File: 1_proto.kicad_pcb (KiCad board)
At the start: 2 copper layers, 229.5 x 77.5 mm, 106 parts, among them K1 KEYSW, K10 KEYSW, K11 KEYSW, K12 KEYSW, K13 KEYSW, K14 KEYSW, K15 KEYSW, K16 KEYSW, K17 KEYSW, K18 KEYSW, K19 KEYSW, K2 KEYSW, K20 KEYSW, K21 KEYSW, K22 KEYSW, K23 KEYSW, K24 KEYSW, K24-A1 KEYSW, K25 KEYSW, K26 KEYSW, K27 KEYSW, K28 KEYSW, K29 KEYSW, K3 KEYSW, K30 KEYSW, K31 KEYSW, K32 KEYSW, K33 KEYSW, K34 KEYSW, K35 KEYSW, K36 KEYSW, K37 KEYSW, K38 KEYSW, K39 KEYSW, K4 KEYSW, K40 KEYSW, K41 KEYSW, K42 KEYSW, K43 KEYSW, K44 KEYSW, K45 KEYSW, K46 KEYSW, K47 KEYSW, K48 KEYSW, K5 KEYSW, K6 KEYSW, K7 KEYSW, K8 KEYSW, K9 KEYSW, SW1 SW_PUSH, U1 ProMicro

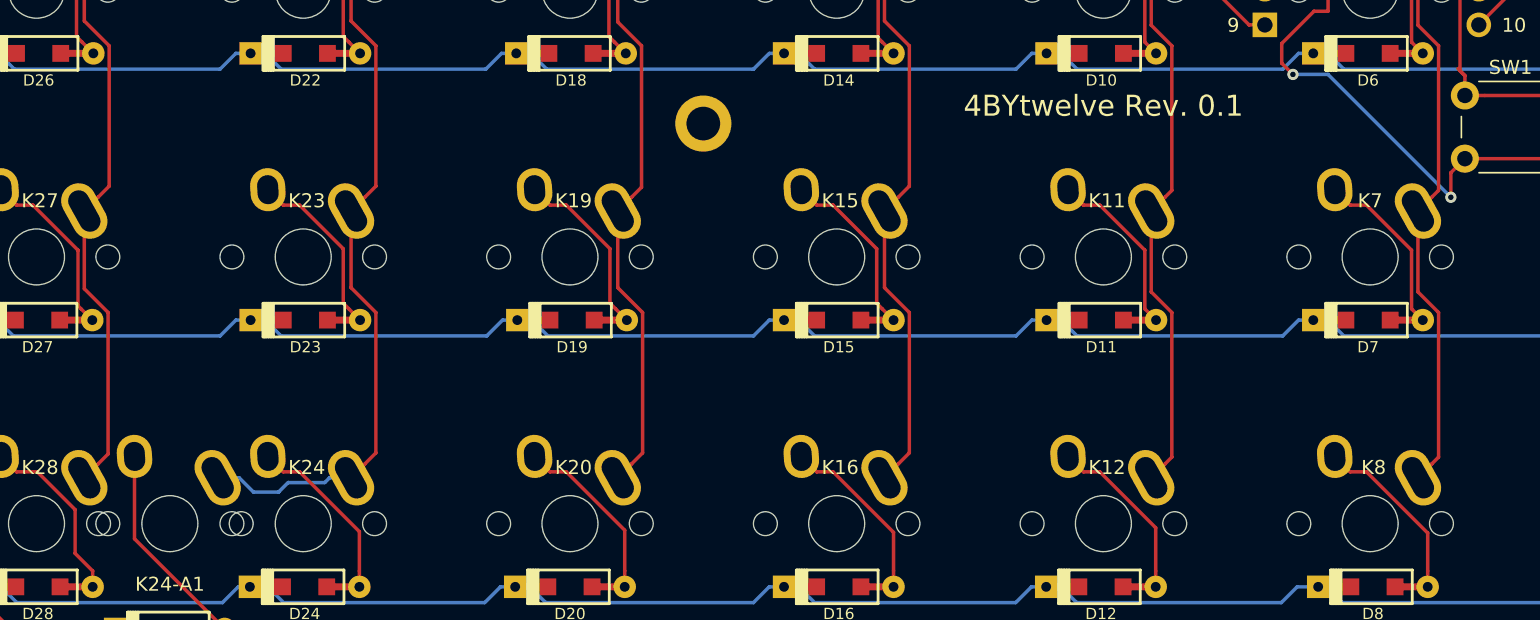
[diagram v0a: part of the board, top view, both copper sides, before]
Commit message: added 2u space key support & minor changes
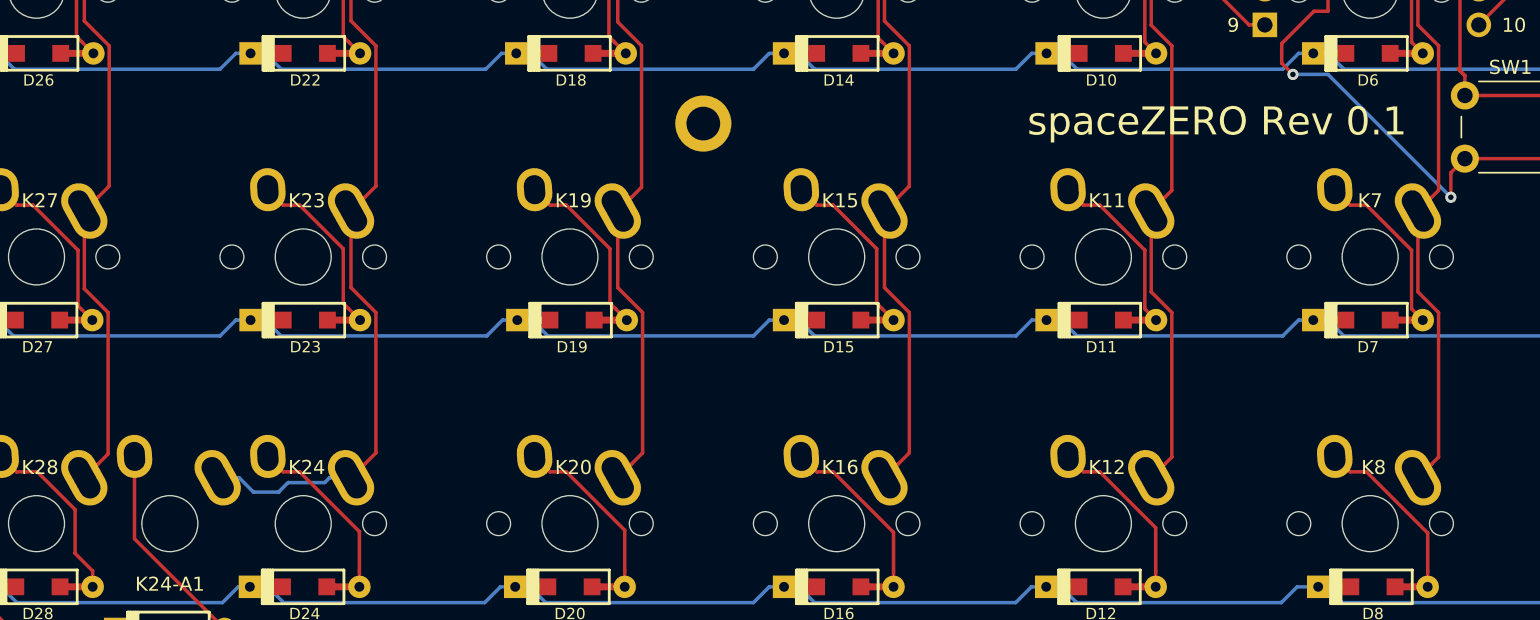
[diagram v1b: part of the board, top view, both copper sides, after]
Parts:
- K24: footprint keebs:Mx_Alps_100 -> locallib:Mx_Alps_100_wo_r_hole
- K24-A1: footprint keebs:Mx_Alps_100 -> locallib:Mx_Alps_100_wide_holes
- K28: footprint keebs:Mx_Alps_100 -> locallib:Mx_Alps_100_wo_l_hole
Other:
- board text added: "spaceZERO Rev 0.1"
- board text removed: "4BYtwelve Rev. 0.1"
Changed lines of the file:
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@@
     (mod_text_size 1 1)
     (mod_text_width 0.15)
-    (pad_size 4 4)
-    (pad_drill 2.4)
+    (pad_size 2.7018 1.7018)
+    (pad_drill 2.7018)
     (pad_to_mask_clearance 0.051)
     (solder_mask_min_width 0.25)
@@
     (add_net row3)
   )
-  (module keebs:Mx_Alps_100 (layer B.Cu)
-    (at 147.5 138.5 180)
+  (module locallib:Mx_Alps_100_wo_l_hole (layer B.Cu)
+    (at 138 138.5 180)
     (descr MXALPS)
     (tags MXALPS)
-    (fp_text reference K24-A1 (at 0 -4.318 180) (layer F.SilkS)
+    (fp_text reference K28 (at -0.25 4 180) (layer F.SilkS)
+      (effects (font (size 1 1) (thickness 0.2)))
+    )
+    (fp_text value KEYSW (at 5.334 -10.922 180) (layer F.SilkS) hide
+      (effects (font (size 1.524 1.524) (thickness 0.3048)))
+    )
+    (fp_line (start -7.62 -7.62) (end -7.62 7.62) (layer Dwgs.User) (width 0.3))
+    (fp_line (start 7.62 -7.62) (end -7.62 -7.62) (layer Dwgs.User) (width 0.3))
+    (fp_line (start 7.62 7.62) (end 7.62 -7.62) (layer Dwgs.User) (width 0.3))
+    (fp_line (start -7.62 7.62) (end 7.62 7.62) (layer Dwgs.User) (width 0.3))
+    (fp_line (start 7.75 6.4) (end -7.75 6.4) (layer Dwgs.User) (width 0.3))
+    (fp_line (start 7.75 -6.4) (end 7.75 6.4) (layer Dwgs.User) (width 0.3))
+    (fp_line (start -7.75 -6.4) (end 7.75 -6.4) (layer Dwgs.User) (width 0.3))
+    (fp_line (start -7.75 -6.4) (end -7.75 6.4) (layer Dwgs.User) (width 0.3))
+    (fp_line (start -6.985 -6.985) (end -6.985 6.985) (layer Eco2.User) (width 0.1524))
+    (fp_line (start 6.985 -6.985) (end -6.985 -6.985) (layer Eco2.User) (width 0.1524))
+    (fp_line (start 6.985 6.985) (end 6.985 -6.985) (layer Eco2.User) (width 0.1524))
+    (fp_line (start -6.985 6.985) (end 6.985 6.985) (layer Eco2.User) (width 0.1524))
+    (fp_line (start -6.35 4.572) (end -6.35 6.35) (layer B.SilkS) (width 0.381))
+    (fp_line (start -6.35 -6.35) (end -6.35 -4.572) (layer B.SilkS) (width 0.381))
+    (fp_line (start -4.572 -6.35) (end -6.35 -6.35) (layer B.SilkS) (width 0.381))
+    (fp_line (start 6.35 -6.35) (end 4.572 -6.35) (layer B.SilkS) (width 0.381))
+    (fp_line (start 6.35 -4.572) (end 6.35 -6.35) (layer B.SilkS) (width 0.381))
+    (fp_line (start 6.35 6.35) (end 6.35 4.572) (layer B.SilkS) (width 0.381))
+    (fp_line (start 4.572 6.35) (end 6.35 6.35) (layer B.SilkS) (width 0.381))
+    (fp_line (start -6.35 6.35) (end -4.572 6.35) (layer B.SilkS) (width 0.381))
+    (fp_line (start -9.398 -9.398) (end -9.398 9.398) (layer Dwgs.User) (width 0.1524))
+    (fp_line (start 9.398 -9.398) (end -9.398 -9.398) (layer Dwgs.User) (width 0.1524))
+    (fp_line (start 9.398 9.398) (end 9.398 -9.398) (layer Dwgs.User) (width 0.1524))
+    (fp_line (start -9.398 9.398) (end 9.398 9.398) (layer Dwgs.User) (width 0.1524))
+    (fp_line (start -6.35 -6.35) (end -6.35 6.35) (layer Cmts.User) (width 0.1524))
+    (fp_line (start 6.35 -6.35) (end -6.35 -6.35) (layer Cmts.User) (width 0.1524))
+    (fp_line (start 6.35 6.35) (end 6.35 -6.35) (layer Cmts.User) (width 0.1524))
+    (fp_line (start -6.35 6.35) (end 6.35 6.35) (layer Cmts.User) (width 0.1524))
+    (pad 2 thru_hole oval (at 2.52 4.79 183.9) (size 2.5 3.08) (drill oval 1.5 2.08) (layers *.Cu *.Mask B.SilkS)
+      (net 32 "Net-(D28-Pad2)"))
+    (pad 1 thru_hole oval (at -3.405 3.27 209.05) (size 2.5 4.17) (drill oval 1.5 3.17) (layers *.Cu *.Mask B.SilkS)
+      (net 59 col6))
+    (pad HOLE np_thru_hole circle (at 5.08 0 180) (size 1.7018 1.7018) (drill 1.7018) (layers *.Cu))
+    (pad HOLE np_thru_hole circle (at 0 0 180) (size 3.9878 3.9878) (drill 3.9878) (layers *.Cu))
+  )
+  (module locallib:Mx_Alps_100_wo_r_hole (layer B.Cu)
+    (at 157 138.5 180)
+    (descr MXALPS)
+    (tags MXALPS)
+    (fp_text reference K24 (at -0.25 4 180) (layer F.SilkS)
       (effects (font (size 1 1) (thickness 0.2)))
     )
@@
     (pad HOLE np_thru_hole circle (at 0 0 180) (size 3.9878 3.9878) (drill 3.9878) (layers *.Cu))
     (pad HOLE np_thru_hole circle (at -5.08 0 180) (size 1.7018 1.7018) (drill 1.7018) (layers *.Cu))
-    (pad HOLE np_thru_hole circle (at 5.08 0 180) (size 1.7018 1.7018) (drill 1.7018) (layers *.Cu))
     (pad 1 thru_hole oval (at -3.405 3.27 209.05) (size 2.5 4.17) (drill oval 1.5 3.17) (layers *.Cu *.Mask B.SilkS)
       (net 58 col5))
     (pad 2 thru_hole oval (at 2.52 4.79 183.9) (size 2.5 3.08) (drill oval 1.5 2.08) (layers *.Cu *.Mask B.SilkS)
-      (net 71 "Net-(D24-A1-Pad2)"))
+      (net 28 "Net-(D24-Pad2)"))
   )
-  (module keebs:Mx_Alps_100 (layer B.Cu)
-    (at 138 138.5 180)
+  (module locallib:Mx_Alps_100_wide_holes (layer B.Cu)
+    (at 147.5 138.5 180)
     (descr MXALPS)
     (tags MXALPS)
-    (fp_text reference K28 (at -0.25 4 180) (layer F.SilkS)
+    (fp_text reference K24-A1 (at 0 -4.318 180) (layer F.SilkS)
       (effects (font (size 1 1) (thickness 0.2)))
     )
@@
     (fp_line (start -6.35 6.35) (end 6.35 6.35) (layer Cmts.User) (width 0.1524))
     (pad 2 thru_hole oval (at 2.52 4.79 183.9) (size 2.5 3.08) (drill oval 1.5 2.08) (layers *.Cu *.Mask B.SilkS)
-      (net 32 "Net-(D28-Pad2)"))
+      (net 71 "Net-(D24-A1-Pad2)"))
     (pad 1 thru_hole oval (at -3.405 3.27 209.05) (size 2.5 4.17) (drill oval 1.5 3.17) (layers *.Cu *.Mask B.SilkS)
-      (net 59 col6))
-    (pad HOLE np_thru_hole circle (at 5.08 0 180) (size 1.7018 1.7018) (drill 1.7018) (layers *.Cu))
-    (pad HOLE np_thru_hole circle (at -5.08 0 180) (size 1.7018 1.7018) (drill 1.7018) (layers *.Cu))
+      (net 58 col5))
+    (pad "" np_thru_hole oval (at 4.75 0 180) (size 2.7018 1.7018) (drill oval 2.7018 1.7018) (layers *.Cu))
+    (pad "" np_thru_hole oval (at -4.75 0 180) (size 2.7018 1.7018) (drill oval 2.7018 1.7018) (layers *.Cu))
     (pad HOLE np_thru_hole circle (at 0 0 180) (size 3.9878 3.9878) (drill 3.9878) (layers *.Cu))
   )
@@
   )
   (module keebs:Mx_Alps_100 (layer B.Cu)
-    (at 157 138.5 180)
-    (descr MXALPS)
-    (tags MXALPS)
-    (fp_text reference K24 (at -0.25 4 180) (layer F.SilkS)
-      (effects (font (size 1 1) (thickness 0.2)))
-    )
-    (fp_text value KEYSW (at 5.334 -10.922 180) (layer F.SilkS) hide
-      (effects (font (size 1.524 1.524) (thickness 0.3048)))
-    )
-    (fp_line (start -6.35 6.35) (end 6.35 6.35) (layer Cmts.User) (width 0.1524))
-    (fp_line (start 6.35 6.35) (end 6.35 -6.35) (layer Cmts.User) (width 0.1524))
-    (fp_line (start 6.35 -6.35) (end -6.35 -6.35) (layer Cmts.User) (width 0.1524))
-    (fp_line (start -6.35 -6.35) (end -6.35 6.35) (layer Cmts.User) (width 0.1524))
-    (fp_line (start -9.398 9.398) (end 9.398 9.398) (layer Dwgs.User) (width 0.1524))
-    (fp_line (start 9.398 9.398) (end 9.398 -9.398) (layer Dwgs.User) (width 0.1524))
-    (fp_line (start 9.398 -9.398) (end -9.398 -9.398) (layer Dwgs.User) (width 0.1524))
-    (fp_line (start -9.398 -9.398) (end -9.398 9.398) (layer Dwgs.User) (width 0.1524))
-    (fp_line (start -6.35 6.35) (end -4.572 6.35) (layer B.SilkS) (width 0.381))
-    (fp_line (start 4.572 6.35) (end 6.35 6.35) (layer B.SilkS) (width 0.381))
-    (fp_line (start 6.35 6.35) (end 6.35 4.572) (layer B.SilkS) (width 0.381))
-    (fp_line (start 6.35 -4.572) (end 6.35 -6.35) (layer B.SilkS) (width 0.381))
-    (fp_line (start 6.35 -6.35) (end 4.572 -6.35) (layer B.SilkS) (width 0.381))
-    (fp_line (start -4.572 -6.35) (end -6.35 -6.35) (layer B.SilkS) (width 0.381))
-    (fp_line (start -6.35 -6.35) (end -6.35 -4.572) (layer B.SilkS) (width 0.381))
-    (fp_line (start -6.35 4.572) (end -6.35 6.35) (layer B.SilkS) (width 0.381))
-    (fp_line (start -6.985 6.985) (end 6.985 6.985) (layer Eco2.User) (width 0.1524))
-    (fp_line (start 6.985 6.985) (end 6.985 -6.985) (layer Eco2.User) (width 0.1524))
-    (fp_line (start 6.985 -6.985) (end -6.985 -6.985) (layer Eco2.User) (width 0.1524))
-    (fp_line (start -6.985 -6.985) (end -6.985 6.985) (layer Eco2.User) (width 0.1524))
-    (fp_line (start -7.75 -6.4) (end -7.75 6.4) (layer Dwgs.User) (width 0.3))
-    (fp_line (start -7.75 -6.4) (end 7.75 -6.4) (layer Dwgs.User) (width 0.3))
-    (fp_line (start 7.75 -6.4) (end 7.75 6.4) (layer Dwgs.User) (width 0.3))
-    (fp_line (start 7.75 6.4) (end -7.75 6.4) (layer Dwgs.User) (width 0.3))
-    (fp_line (start -7.62 7.62) (end 7.62 7.62) (layer Dwgs.User) (width 0.3))
-    (fp_line (start 7.62 7.62) (end 7.62 -7.62) (layer Dwgs.User) (width 0.3))
-    (fp_line (start 7.62 -7.62) (end -7.62 -7.62) (layer Dwgs.User) (width 0.3))
-    (fp_line (start -7.62 -7.62) (end -7.62 7.62) (layer Dwgs.User) (width 0.3))
-    (pad HOLE np_thru_hole circle (at 0 0 180) (size 3.9878 3.9878) (drill 3.9878) (layers *.Cu))
-    (pad HOLE np_thru_hole circle (at -5.08 0 180) (size 1.7018 1.7018) (drill 1.7018) (layers *.Cu))
-    (pad HOLE np_thru_hole circle (at 5.08 0 180) (size 1.7018 1.7018) (drill 1.7018) (layers *.Cu))
-    (pad 1 thru_hole oval (at -3.405 3.27 209.05) (size 2.5 4.17) (drill oval 1.5 3.17) (layers *.Cu *.Mask B.SilkS)
-      (net 58 col5))
-    (pad 2 thru_hole oval (at 2.52 4.79 183.9) (size 2.5 3.08) (drill oval 1.5 2.08) (layers *.Cu *.Mask B.SilkS)
-      (net 28 "Net-(D24-Pad2)"))
-  )
-  (module keebs:Mx_Alps_100 (layer B.Cu)
     (at 138 81.5 180)
     (descr MXALPS)
@@
     (effects (font (size 1 1) (thickness 0.1)))
   )
-  (gr_text "4BYtwelve Rev. 0.1" (at 214 108.75) (layer F.SilkS)
-    (effects (font (size 1.5 1.5) (thickness 0.3)))
+  (gr_text "spaceZERO Rev 0.1" (at 222.1 109.85) (layer F.SilkS)
+    (effects (font (size 2 2) (thickness 0.4)))
   )
   (gr_text "ProMicro \nhere!" (at 233.75 90.25) (layer F.SilkS)
     (effects (font (size 1 1) (thickness 0.2)))
   )
-  (gr_text "4BYtwelve Rev. 0.1" (at 241.5 146.5) (layer B.SilkS)
+  (gr_text "spaceZERO Rev 0.1" (at 241.5 146.5) (layer B.SilkS)
     (effects (font (size 2 2) (thickness 0.3)) (justify mirror))
   )

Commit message: release SpaceZERO Rev 0.1
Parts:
- added G***: LOGO, 1_proto:spaceZEROlogo, B.Cu at (100.1, 129.3)
- added G***: LOGO, 1_proto:spaceZEROlogo_small, F.Cu at (182.2, 98.2)
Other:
- rule via_min_size: 0.4 -> 0.3
- board text added: "Rev 0.1"
- board text removed: "spaceZERO Rev 0.1"
